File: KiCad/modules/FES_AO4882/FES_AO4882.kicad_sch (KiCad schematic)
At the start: 42 parts, among them J10 Conn_01x01_Pin, J11 Conn_01x01_Pin, J12 Conn_01x01_Pin, J13 Conn_01x01_Pin, J14 Conn_01x01_Pin, J15 Conn_01x01_Pin, J16 Conn_01x01_Pin, J17 Conn_01x01_Pin, J18 Conn_01x01_Pin, J19 Conn_01x01_Pin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

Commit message: cleaned all modules + production files
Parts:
- J11, J12, J13, J14, J20, J21, J22, J23: now not fitted; now left out of the parts list
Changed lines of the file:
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@@
 		(unit 1)
 		(exclude_from_sim no)
-		(in_bom yes)
+		(in_bom no)
 		(on_board yes)
-		(dnp no)
+		(dnp yes)
 		(property "Reference" "J12"
 			(at 232.41 78.74 0)
@@
 		(unit 1)
 		(exclude_from_sim no)
-		(in_bom yes)
+		(in_bom no)
 		(on_board yes)
-		(dnp no)
+		(dnp yes)
 		(property "Reference" "J11"
 			(at 232.41 76.2 0)
@@
 		(unit 1)
 		(exclude_from_sim no)
-		(in_bom yes)
+		(in_bom no)
 		(on_board yes)
-		(dnp no)
+		(dnp yes)
 		(property "Reference" "J13"
 			(at 232.41 81.28 0)
@@
 		(at 232.41 113.03 180)
 		(unit 1)
-		(exclude_from_sim no)
-		(in_bom yes)
+		(exclude_from_sim yes)
+		(in_bom no)
 		(on_board yes)
-		(dnp no)
+		(dnp yes)
 		(property "Reference" "J20"
 			(at 232.41 111.76 0)
@@
 		(at 232.41 120.65 180)
 		(unit 1)
-		(exclude_from_sim no)
-		(in_bom yes)
+		(exclude_from_sim yes)
+		(in_bom no)
 		(on_board yes)
-		(dnp no)
+		(dnp yes)
 		(property "Reference" "J23"
 			(at 232.41 119.38 0)
@@
 		(unit 1)
 		(exclude_from_sim no)
-		(in_bom yes)
+		(in_bom no)
 		(on_board yes)
-		(dnp no)
+		(dnp yes)
 		(property "Reference" "J14"
 			(at 232.41 83.82 0)
@@
 		(at 232.41 115.57 180)
 		(unit 1)
-		(exclude_from_sim no)
-		(in_bom yes)
+		(exclude_from_sim yes)
+		(in_bom no)
 		(on_board yes)
-		(dnp no)
+		(dnp yes)
 		(property "Reference" "J21"
 			(at 232.41 114.3 0)
@@
 		(at 232.41 118.11 180)
 		(unit 1)
-		(exclude_from_sim no)
-		(in_bom yes)
+		(exclude_from_sim yes)
+		(in_bom no)
 		(on_board yes)
-		(dnp no)
+		(dnp yes)
 		(property "Reference" "J22"
 			(at 232.41 116.84 0)

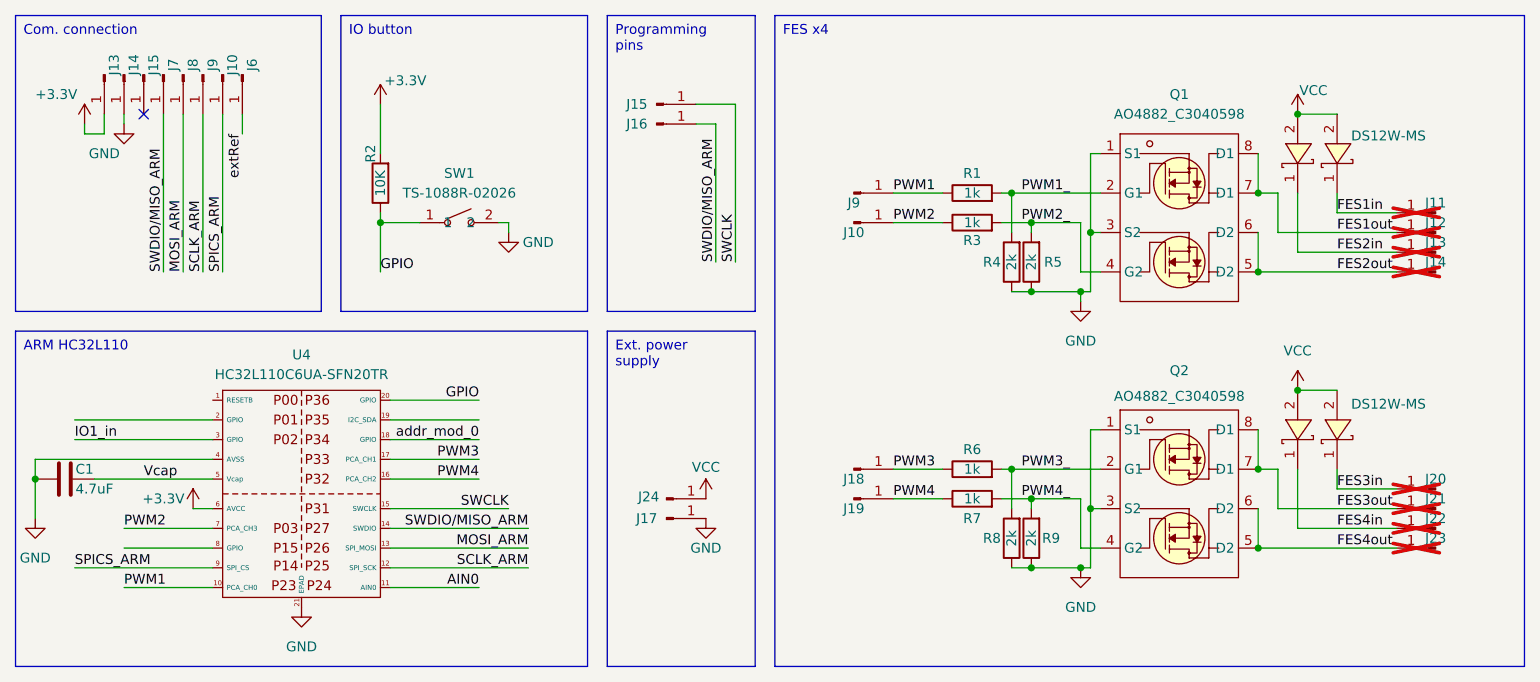
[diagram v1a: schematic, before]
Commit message: renamed SPI buses
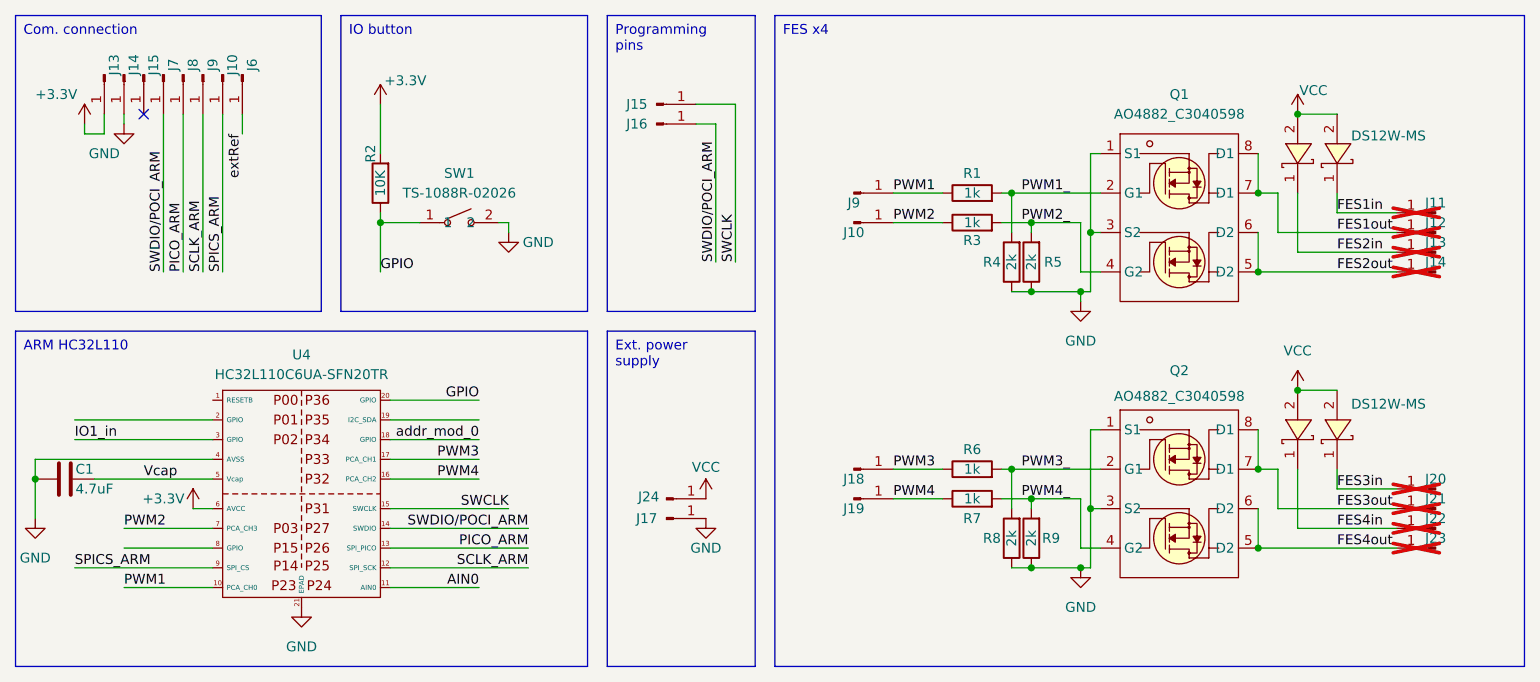
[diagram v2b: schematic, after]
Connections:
- net MOSI_ARM renamed PICO_ARM
- net SWDIO/MISO_ARM renamed SWDIO/POCI_ARM
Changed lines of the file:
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@@
 		)
 	)
-	(label "SWDIO{slash}MISO_ARM"
+	(label "SWDIO{slash}POCI_ARM"
 		(at 139.7 83.82 90)
 		(fields_autoplaced yes)
@@
 		)
 	)
-	(label "SWDIO{slash}MISO_ARM"
+	(label "SWDIO{slash}POCI_ARM"
 		(at 115.57 118.11 180)
 		(fields_autoplaced yes)
@@
 		)
 	)
-	(label "MOSI_ARM"
+	(label "PICO_ARM"
 		(at 71.12 85.09 90)
 		(fields_autoplaced yes)
@@
 		)
 	)
-	(label "SWDIO{slash}MISO_ARM"
+	(label "SWDIO{slash}POCI_ARM"
 		(at 68.58 85.09 90)
 		(fields_autoplaced yes)
@@
 		)
 	)
-	(label "MOSI_ARM"
+	(label "PICO_ARM"
 		(at 115.57 120.65 180)
 		(fields_autoplaced yes)
@@
 		)
 		(pin "13"
-			(alternate "SPI_MOSI")
+			(alternate "SPI_PICO")
 		)
 		(pin "11"
